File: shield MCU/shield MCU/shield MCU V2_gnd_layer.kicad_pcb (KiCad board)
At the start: 2 copper layers, 56 x 75.2 mm, 16 parts, among them J1 IR_sensor, J2 IR_sensor, J3 IR_sensor, J4 IR_sensor, J5 IR_sensor, J6 BATT, SW1 Pwr_Sw, U1 pwr_mgr_1, U3 gy50, U4 NUCLEO144-F429ZI

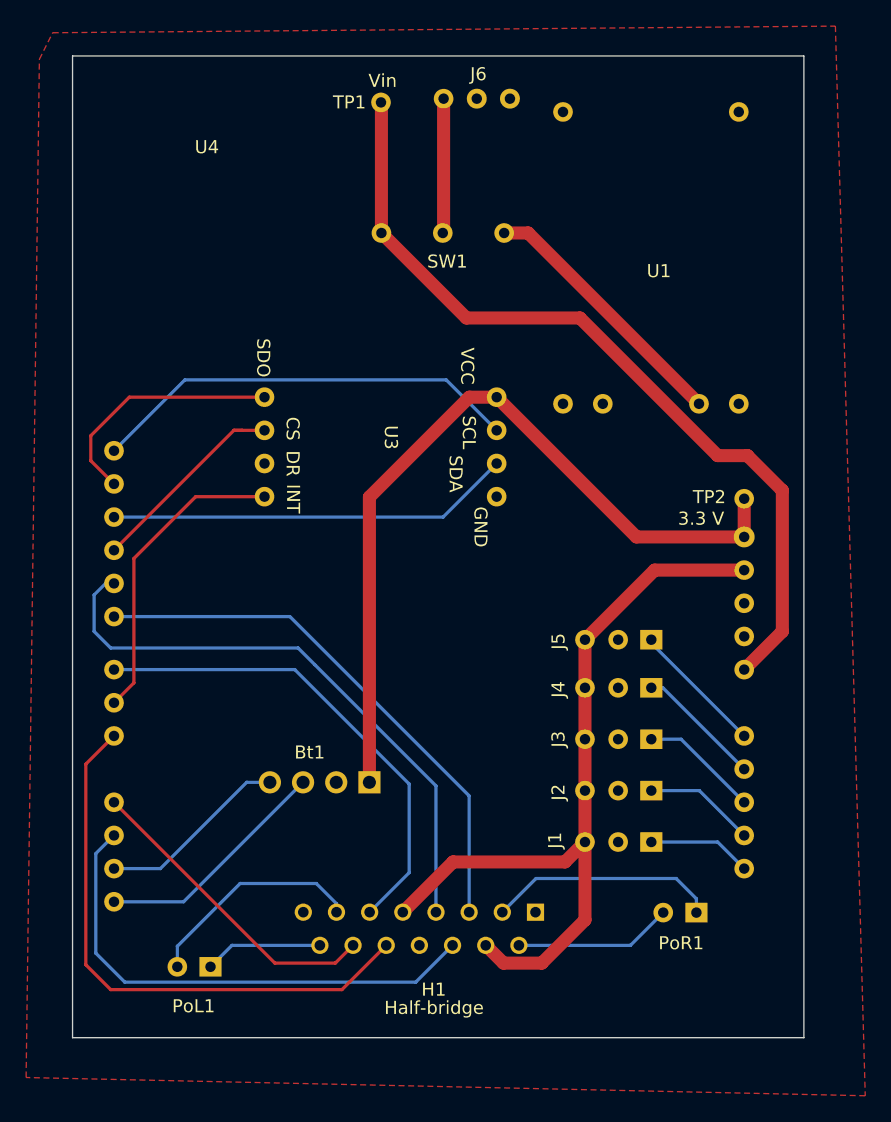
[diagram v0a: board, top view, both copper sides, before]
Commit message: PCB päivitetty
switchien VIA koot muutettu ja L298N footprint päivitetty
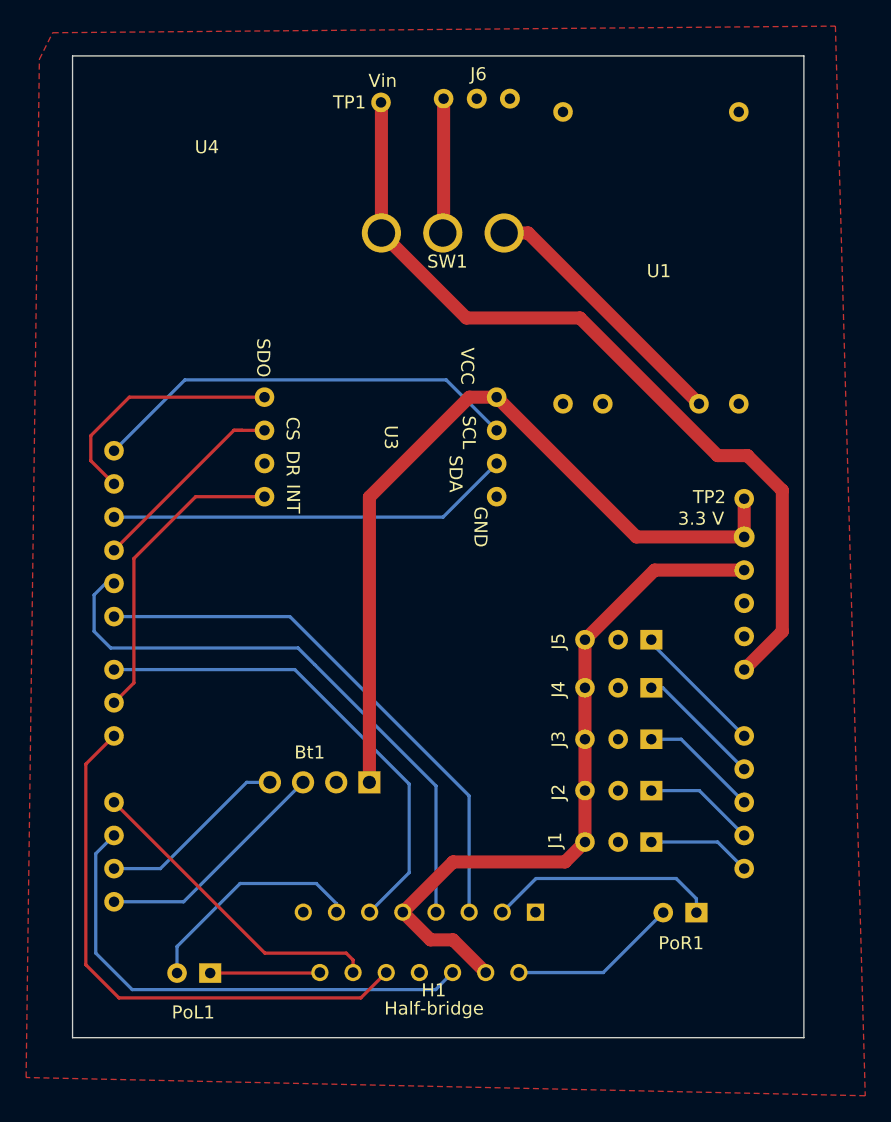
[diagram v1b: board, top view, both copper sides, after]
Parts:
- moved PoL1 0.48 mm to (113.5, 136.1)
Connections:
- U4 pad 108: Net-(J4-Pad1) -> Net-(J1-Pad1)
- U4 pad 130: Net-(J3-Pad1) -> Net-(J2-Pad1)
- U4 pad 37: Net-(J2-Pad1) -> Net-(J3-Pad1)
- U4 pad 38: Net-(J1-Pad1) -> Net-(J4-Pad1)
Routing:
- net /5V: track 61.6 -> 54.3 mm
- net Net-(J4-Pad1): track 7.95 -> 9.69 mm
- net Net-(J1-Pad1): track 9.69 -> 7.95 mm
- net Net-(H1-Pad2): track 12.1 -> 13.0 mm
- net Net-(H1-Pad14): track 9.06 -> 8.36 mm
- net Net-(J3-Pad1): track 8.53 -> 9.11 mm
- net Net-(J2-Pad1): track 9.11 -> 8.53 mm

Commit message: uus pcb
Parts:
- added REF**: SPDT_rec, Omat:SPDT_rec, F.Cu at (105.3, 77.5)
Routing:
- added copper zone on B.Cu, net GND
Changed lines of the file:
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@@
       (drillshape 0)
       (scaleselection 1)
-      (outputdirectory "")
+      (outputdirectory "Sulari gerber/")
     )
   )
@@
       (effects (font (size 1 1) (thickness 0.15)))
     )
-    (pad "1" thru_hole circle (at 11.303 -4.064 180) (size 3 3) (drill 2.1) (layers *.Cu *.Mask)
+    (pad "1" thru_hole circle (at 11.303 -4.064 180) (size 1.5 1.5) (drill 0.8) (layers *.Cu *.Mask)
       (net 18 "/Vin") (pinfunction "A") (pintype "passive"))
-    (pad "2" thru_hole circle (at 6.604 -4.064 180) (size 3 3) (drill 2.1) (layers *.Cu *.Mask)
+    (pad "2" thru_hole circle (at 6.604 -4.064 180) (size 1.5 1.5) (drill 0.8) (layers *.Cu *.Mask)
       (net 20 "/Batt+") (pinfunction "B") (pintype "passive"))
-    (pad "3" thru_hole circle (at 1.905 -4.064 180) (size 3 3) (drill 2.1) (layers *.Cu *.Mask)
+    (pad "3" thru_hole circle (at 1.905 -4.064 180) (size 1.5 1.5) (drill 0.8) (layers *.Cu *.Mask)
       (net 19 "/chrg+") (pinfunction "C") (pintype "passive"))
   )
@@
     (pad "6" thru_hole circle (at 2.54 -15.24 270) (size 1.5 1.5) (drill 0.8) (layers *.Cu *.Mask)
       (net 16 "unconnected-(U1-Pad6)") (pinfunction "in+") (pintype "no_connect"))
+  )
+  (footprint "Omat:SPDT_rec" (layer "F.Cu")
+    (at 105.283 77.47)
+    (attr through_hole)
+    (fp_text reference "REF**" (at 6.985 0.508 unlocked) (layer "F.SilkS")
+      (effects (font (size 1 1) (thickness 0.15)))
+    )
+    (fp_text value "SPDT_rec" (at 6.858 2.413 unlocked) (layer "F.Fab")
+      (effects (font (size 1 1) (thickness 0.15)))
+    )
+    (fp_text user "${REFERENCE}" (at 6.35 3.937 unlocked) (layer "F.Fab")
+      (effects (font (size 1 1) (thickness 0.15)))
+    )
+    (fp_rect (start 4.572 -1.9812) (end 15.5448 -8.0264) (layer "Edge.Cuts") (width 0.12) (fill none))
+    (fp_circle (center 18.542 -4.986049) (end 19.304 -4.325649) (layer "Edge.Cuts") (width 0.12) (fill none))
+    (fp_circle (center 1.5748 -4.988612) (end 2.286 -4.277412) (layer "Edge.Cuts") (width 0.12) (fill none))
   )
   (footprint "Connector_Pin:Pin_D0.7mm_L6.5mm_W1.8mm_FlatFork" (layer "F.Cu")
@@
       )
     )
+  )
+  (zone (net 1) (net_name "GND") (layer "B.Cu") (hatch edge 0.508)
+    (connect_pads (clearance 0.508))
+    (min_thickness 0.254) (filled_areas_thickness no)
+    (fill yes (thermal_gap 0.508) (thermal_bridge_width 0.508))
+    (polygon
+      (pts
+        (xy 103.632 65.786)
+        (xy 159.131 65.659)
+        (xy 158.623 141.097)
+        (xy 102.87 141.097)
+        (xy 102.997 65.532)
+      )
+    )
